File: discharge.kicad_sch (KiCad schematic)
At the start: 6 parts, among them J10 XT30_F, K1 G5LE-1

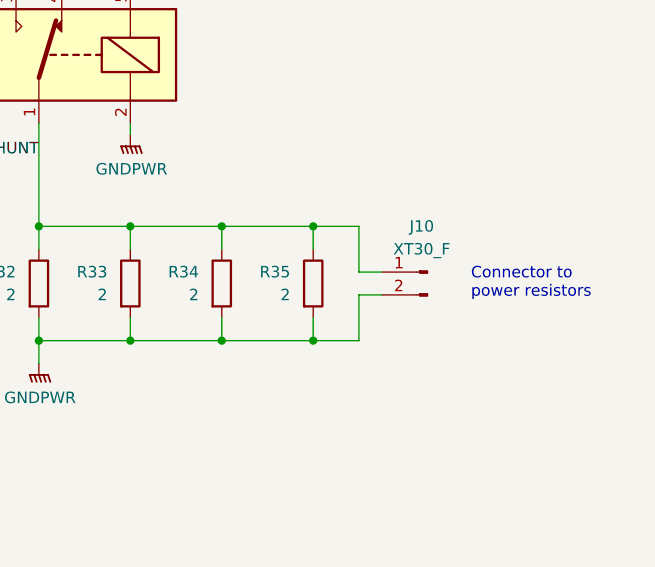
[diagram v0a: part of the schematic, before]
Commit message: Specc'd all components + started creating rev 1b boards
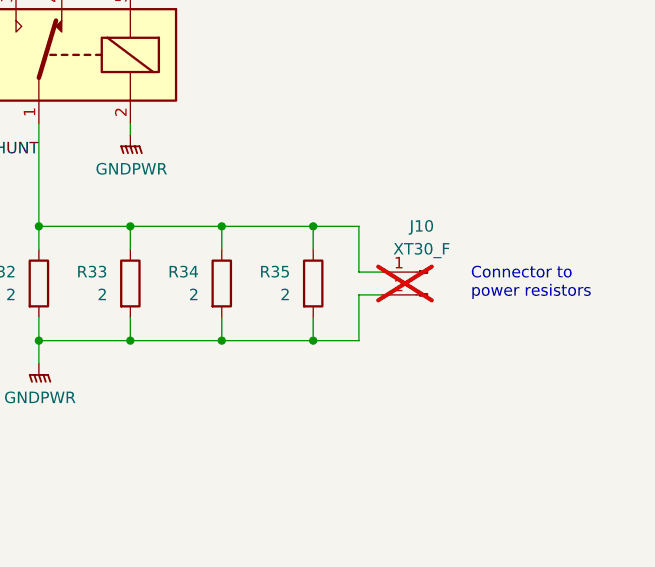
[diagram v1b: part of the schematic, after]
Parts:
- J10: now not fitted
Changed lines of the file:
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@@
 		(in_bom yes)
 		(on_board yes)
-		(dnp no)
+		(dnp yes)
 		(property "Reference" "J10"
 			(at 139.065 72.39 0)
